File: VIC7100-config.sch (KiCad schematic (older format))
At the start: 47 parts, among them J1 TAG-10PIN, Q1 DMG1013UWQ-7, U13 VIC7100, U2 GD25LQ256DWIGR, U7 STM811RW16F, Y2 ABM8G-25.000MHZ-18-D2Y-T, Y3 ABM8G-27.000MHZ-18-D2Y-T

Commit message: RGMII sketch, started LCD
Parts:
- U2: footprint arvsom-footprints:8-WSON-6x5 -> antmicro-footprints:GD25Q16CWIG
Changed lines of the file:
@@
 AR Path="/607858CA/60ADDC66" Ref="U?"  Part="1"
 AR Path="/60805CC6/60ADDC66" Ref="U2"  Part="1"
+AR Path="/60ADDC66" Ref="U2"  Part="1"
 F 0 "U2" H 11325 6080 50  0000 C CNN
 F 1 "GD25LQ256DWIGR" H 11325 5989 50  0000 C CNN
-F 2 "arvsom-footprints:8-WSON-6x5" H 10925 5925 50  0001 C CNN
+F 2 "antmicro-footprints:GD25Q16CWIG" H 10925 5925 50  0001 C CNN
 F 3 "" H 10925 5925 50  0001 C CNN
 F 4 "GD25LQ256DWIGR" H 11325 5898 50  0001 C CNN "MPN"

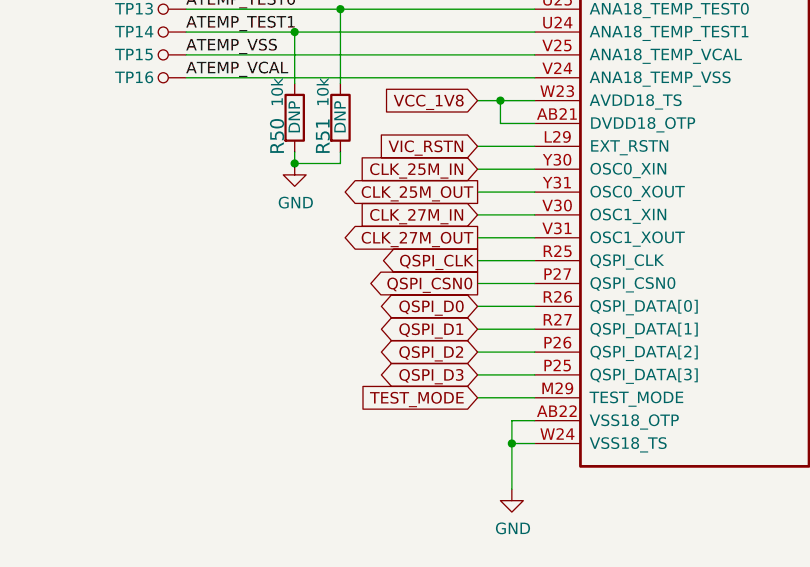
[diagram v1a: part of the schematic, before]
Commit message: Routed USB, QSPI, JTAG
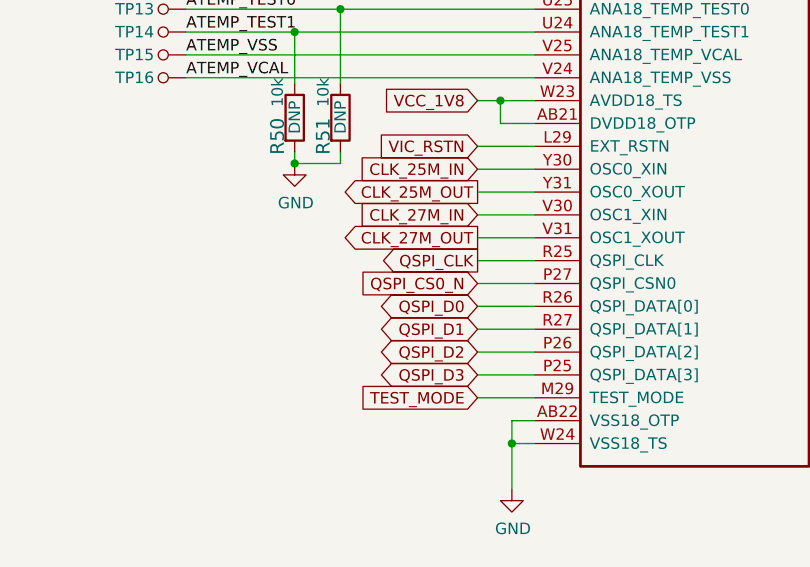
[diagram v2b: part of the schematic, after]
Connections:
- net QSPI_CSN0 is gone; now on net QSPI_CS0_N: U13.P27 (QSPI_CSN0)
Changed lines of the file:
@@
 Text GLabel 6150 3450 0    50   Output ~ 0
 QSPI_CLK
-Text GLabel 6150 3550 0    50   Output ~ 0
-QSPI_CSN0
 Text GLabel 6150 3650 0    50   BiDi ~ 0
 QSPI_D0
@@
 	0    1    1    0
 $EndComp
+Text GLabel 6150 3550 0    50   Input ~ 0
+QSPI_CS0_N
 $EndSCHEMATC

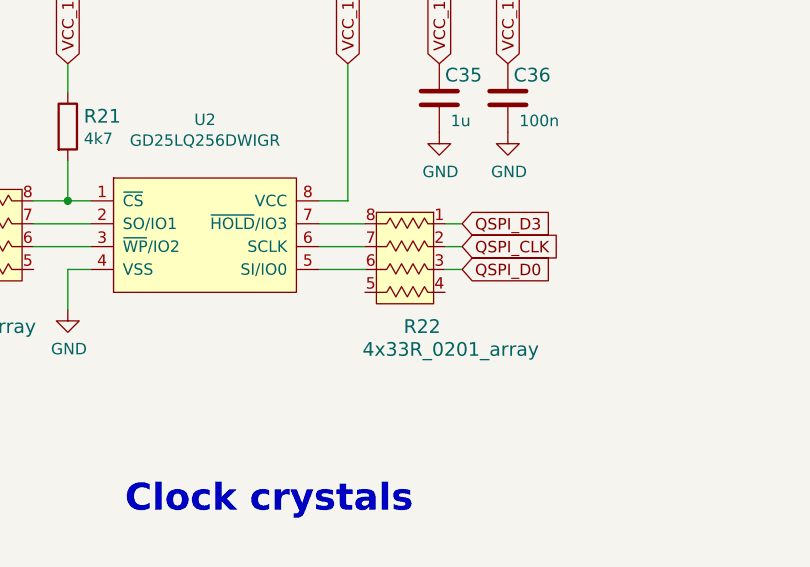
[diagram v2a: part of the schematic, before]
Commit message: PMIC re-worked, layout
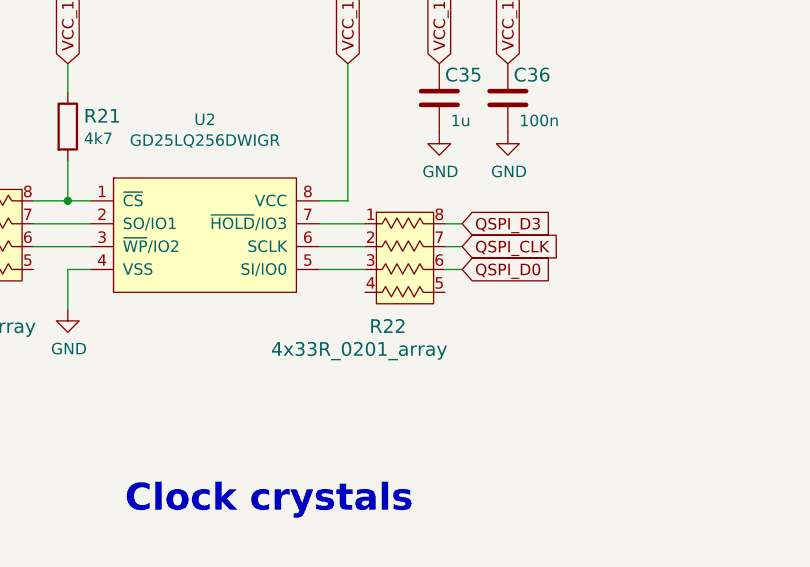
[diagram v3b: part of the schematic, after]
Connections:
- net QSPI_CLK: now also R22.7; no longer R22.2
- net QSPI_D0: now also R22.6; no longer R22.3
- net QSPI_D3: now also R22.8; no longer R22.1
- net at U2.5 (SI/IO0): now also R22.3; no longer R22.6
- net at U2.6 (SCLK): now also R22.2; no longer R22.7
- net at U2.7 (~HOLD~/IO3): now also R22.1; no longer R22.8
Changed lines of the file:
@@
 L arvsom:4x33R_0201_array R22
 U 1 1 609DE671
-P 12175 6625
-F 0 "R22" H 12075 6575 60  0000 C CNN
-F 1 "4x33R_0201_array" H 11950 6475 60  0000 C CNN
-F 2 "arvsom-footprints:EXB18V" H 11975 7375 60  0001 L CNN
-F 3 "http://industrial.panasonic.com/cdbs/www-data/pdf/AOC0000/AOC0000C14.pdf" H 11975 7375 60  0001 L CNN
-F 4 "EXB-18V330JX" H 11975 7575 60  0001 L CNN "MPN"
-F 5 "Panasonic" H 11975 7475 60  0001 L CNN "Manufacturer"
-	1    12175 6625
-	-1   0    0    -1
-$EndComp
-Wire Wire Line
-	11825 6225 12025 6225
-Wire Wire Line
-	11825 6325 12025 6325
-Wire Wire Line
-	11825 6425 12025 6425
+P 12225 6625
+F 0 "R22" H 12125 6575 60  0000 C CNN
+F 1 "4x33R_0201_array" H 12000 6475 60  0000 C CNN
+F 2 "arvsom-footprints:EXB18V" H 12025 7375 60  0001 L CNN
+F 3 "http://industrial.panasonic.com/cdbs/www-data/pdf/AOC0000/AOC0000C14.pdf" H 12025 7375 60  0001 L CNN
+F 4 "EXB-18V330JX" H 12025 7575 60  0001 L CNN "MPN"
+F 5 "Panasonic" H 12025 7475 60  0001 L CNN "Manufacturer"
+	1    12225 6625
+	1    0    0    -1
+$EndComp
 $Comp
 L arvsom:4x33R_0201_array R18
@@
 Text GLabel 6150 3550 0    50   Input ~ 0
 QSPI_CS0_N
+Wire Wire Line
+	11825 6225 12025 6225
+Wire Wire Line
+	11825 6325 12025 6325
+Wire Wire Line
+	11825 6425 12025 6425
 $EndSCHEMATC

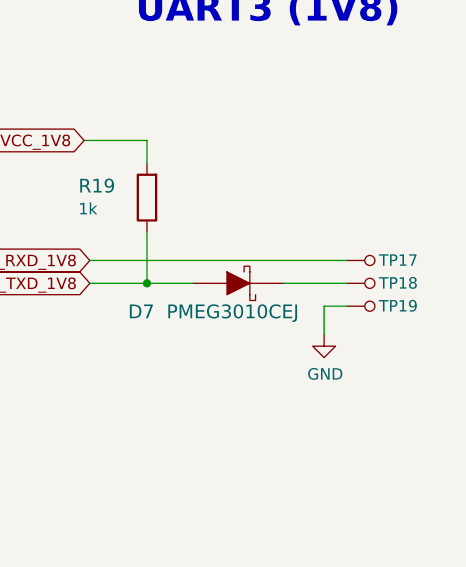
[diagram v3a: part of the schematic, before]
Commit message: Layout: 5v8 dcdc, clocks, SPIFlash, testpoints
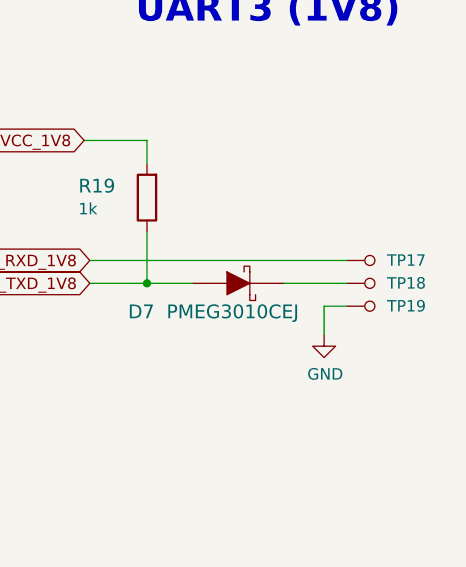
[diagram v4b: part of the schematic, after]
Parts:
- removed TP17, TP18, TP19: TP_SMD_0_75MM, arvsom-footprints:Testpoint_smd_0_75mm, symbol arvsom:TP_SMD_0_75MM
- added TP17, TP18, TP19: TP_SMD1MM, arvsom-footprints:Testpoint_smd_1mm, symbol arvsom:TP_SMD1MM
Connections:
- net GND: now also TP19.1
- net UART3_RXD_1V8: now also TP17.1
- net at D7.K: now also TP18.1
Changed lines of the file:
@@
 Text Notes 13250 1525 0    118  ~ 24
 UART3 (1V8)
-$Comp
-L arvsom:TP_SMD_0_75MM TP19
-U 1 1 60A17308
-P 14275 2750
-F 0 "TP19" V 14275 2625 50  0000 C CNN
-F 1 "TP_SMD_0_75MM" H 14275 2650 50  0001 C CNN
-F 2 "arvsom-footprints:Testpoint_smd_0_75mm" H 14475 2950 60  0001 L CNN
-F 3 "" H 14475 3050 60  0001 L CNN
-	1    14275 2750
-	0    -1   -1   0
-$EndComp
-$Comp
-L arvsom:TP_SMD_0_75MM TP18
-U 1 1 60A1730E
-P 14275 2650
-F 0 "TP18" V 14275 2525 50  0000 C CNN
-F 1 "TP_SMD_0_75MM" H 14275 2550 50  0001 C CNN
-F 2 "arvsom-footprints:Testpoint_smd_0_75mm" H 14475 2850 60  0001 L CNN
-F 3 "" H 14475 2950 60  0001 L CNN
-	1    14275 2650
-	0    -1   -1   0
-$EndComp
-$Comp
-L arvsom:TP_SMD_0_75MM TP17
-U 1 1 60A17314
-P 14275 2550
-F 0 "TP17" V 14275 2425 50  0000 C CNN
-F 1 "TP_SMD_0_75MM" H 14275 2450 50  0001 C CNN
-F 2 "arvsom-footprints:Testpoint_smd_0_75mm" H 14475 2750 60  0001 L CNN
-F 3 "" H 14475 2850 60  0001 L CNN
-	1    14275 2550
-	0    -1   -1   0
-$EndComp
 Wire Wire Line
 	14175 2750 14075 2750
@@
 Wire Wire Line
 	11825 6425 12025 6425
+$Comp
+L arvsom:TP_SMD1MM TP?
+U 1 1 60E73BC7
+P 14275 2550
+AR Path="/613A40EE/60E73BC7" Ref="TP?"  Part="1"
+AR Path="/60805CC6/60E73BC7" Ref="TP17"  Part="1"
+F 0 "TP17" V 14275 2475 50  0000 R CNN
+F 1 "TP_SMD1MM" H 14275 2450 50  0001 C CNN
+F 2 "arvsom-footprints:Testpoint_smd_1mm" H 14475 2750 60  0001 L CNN
+F 3 "" H 14475 2850 60  0001 L CNN
+	1    14275 2550
+	0    -1   -1   0
+$EndComp
+$Comp
+L arvsom:TP_SMD1MM TP?
+U 1 1 60E7D537
+P 14275 2650
+AR Path="/613A40EE/60E7D537" Ref="TP?"  Part="1"
+AR Path="/60805CC6/60E7D537" Ref="TP18"  Part="1"
+F 0 "TP18" V 14275 2575 50  0000 R CNN
+F 1 "TP_SMD1MM" H 14275 2550 50  0001 C CNN
+F 2 "arvsom-footprints:Testpoint_smd_1mm" H 14475 2850 60  0001 L CNN
+F 3 "" H 14475 2950 60  0001 L CNN
+	1    14275 2650
+	0    -1   -1   0
+$EndComp
+$Comp
+L arvsom:TP_SMD1MM TP?
+U 1 1 60E7D732
+P 14275 2750
+AR Path="/613A40EE/60E7D732" Ref="TP?"  Part="1"
+AR Path="/60805CC6/60E7D732" Ref="TP19"  Part="1"
+F 0 "TP19" V 14275 2675 50  0000 R CNN
+F 1 "TP_SMD1MM" H 14275 2650 50  0001 C CNN
+F 2 "arvsom-footprints:Testpoint_smd_1mm" H 14475 2950 60  0001 L CNN
+F 3 "" H 14475 3050 60  0001 L CNN
+	1    14275 2750
+	0    -1   -1   0
+$EndComp
 $EndSCHEMATC

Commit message: Update libs
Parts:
- U2: footprint antmicro-footprints:GD25Q16CWIG -> arvsom-footprints:GD25Q16CWIG
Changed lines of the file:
@@
 F 0 "U2" H 11325 6080 50  0000 C CNN
 F 1 "GD25LQ256DWIGR" H 11325 5989 50  0000 C CNN
-F 2 "antmicro-footprints:GD25Q16CWIG" H 10925 5925 50  0001 C CNN
+F 2 "arvsom-footprints:GD25Q16CWIG" H 10925 5925 50  0001 C CNN
 F 3 "" H 10925 5925 50  0001 C CNN
 F 4 "GD25LQ256DWIGR" H 11325 5898 50  0001 C CNN "MPN"

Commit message: Update lib attributes
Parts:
- J1: MPN (none) -> TC2050-IDC-NL; Manufacturer (none) -> Tag-Connect
- U9: renamed from U2; Manufacturer (none) -> GigaDevice
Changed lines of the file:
@@
 P 10925 5925
 AR Path="/607858CA/60ADDC66" Ref="U?"  Part="1"
-AR Path="/60805CC6/60ADDC66" Ref="U2"  Part="1"
+AR Path="/60805CC6/60ADDC66" Ref="U9"  Part="1"
 AR Path="/60ADDC66" Ref="U2"  Part="1"
-F 0 "U2" H 11325 6080 50  0000 C CNN
+F 0 "U9" H 11325 6080 50  0000 C CNN
 F 1 "GD25LQ256DWIGR" H 11325 5989 50  0000 C CNN
 F 2 "arvsom-footprints:GD25Q16CWIG" H 10925 5925 50  0001 C CNN
 F 3 "" H 10925 5925 50  0001 C CNN
 F 4 "GD25LQ256DWIGR" H 11325 5898 50  0001 C CNN "MPN"
+F 5 "GigaDevice" H 10925 5925 50  0001 C CNN "Manufacturer"
 	1    10925 5925
 	1    0    0    -1
@@
 F 2 "arvsom-footprints:Tag-Connect_TC2050-IDC-NL" H 10150 2450 50  0001 L BNN
 F 3 "" H 10400 2450 50  0001 L BNN
+F 4 "TC2050-IDC-NL" H 10450 1975 50  0000 C CNN "MPN"
+F 5 "Tag-Connect" H 10400 2450 50  0001 C CNN "Manufacturer"
 	1    10400 2450
 	1    0    0    -1
